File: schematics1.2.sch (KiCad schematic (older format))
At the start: 26 parts, among them J1 Keypad, SW1 SW_SPST, SW2 SW_SPST, SW3 SW_SPST, SW4 SW_SPST, U1 EA_T123X-I2C

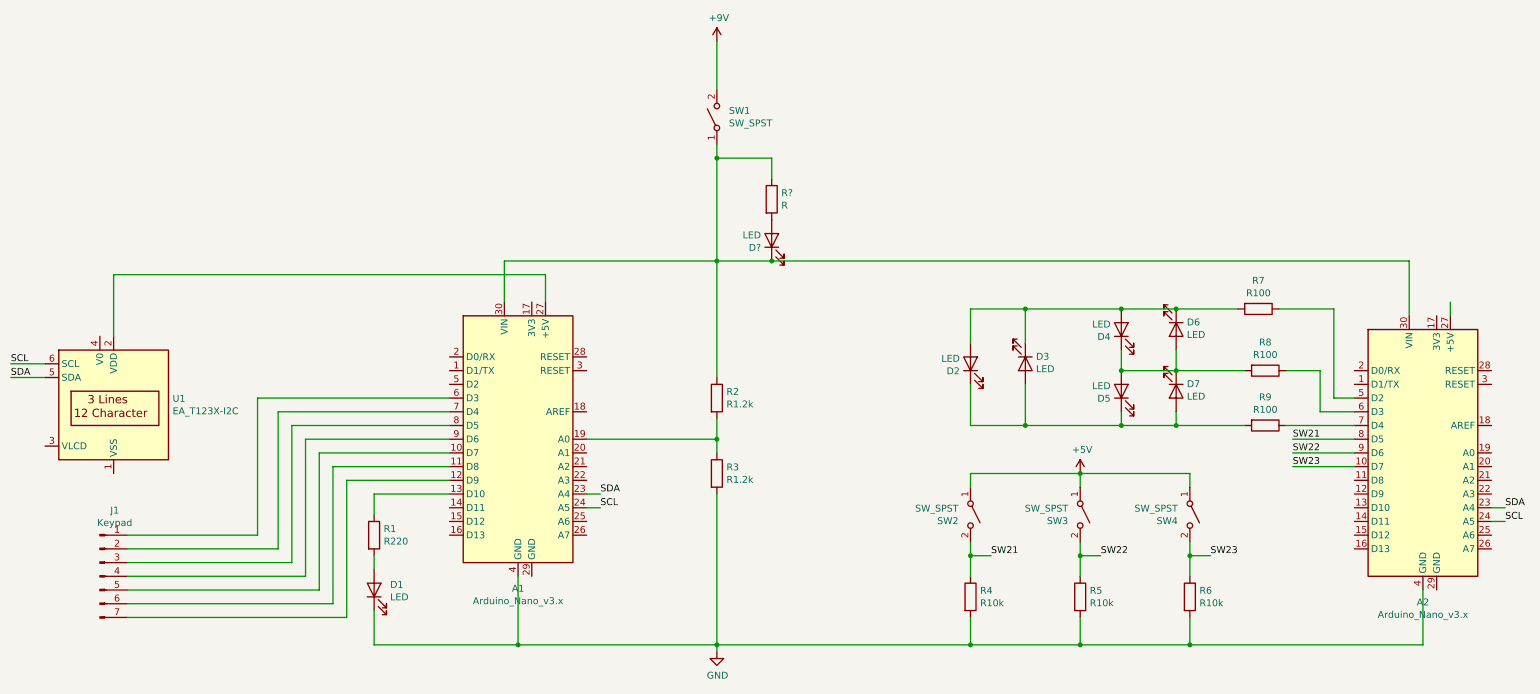
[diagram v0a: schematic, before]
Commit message: Removed second Nano, moved all components onto the one board. The second board is not required
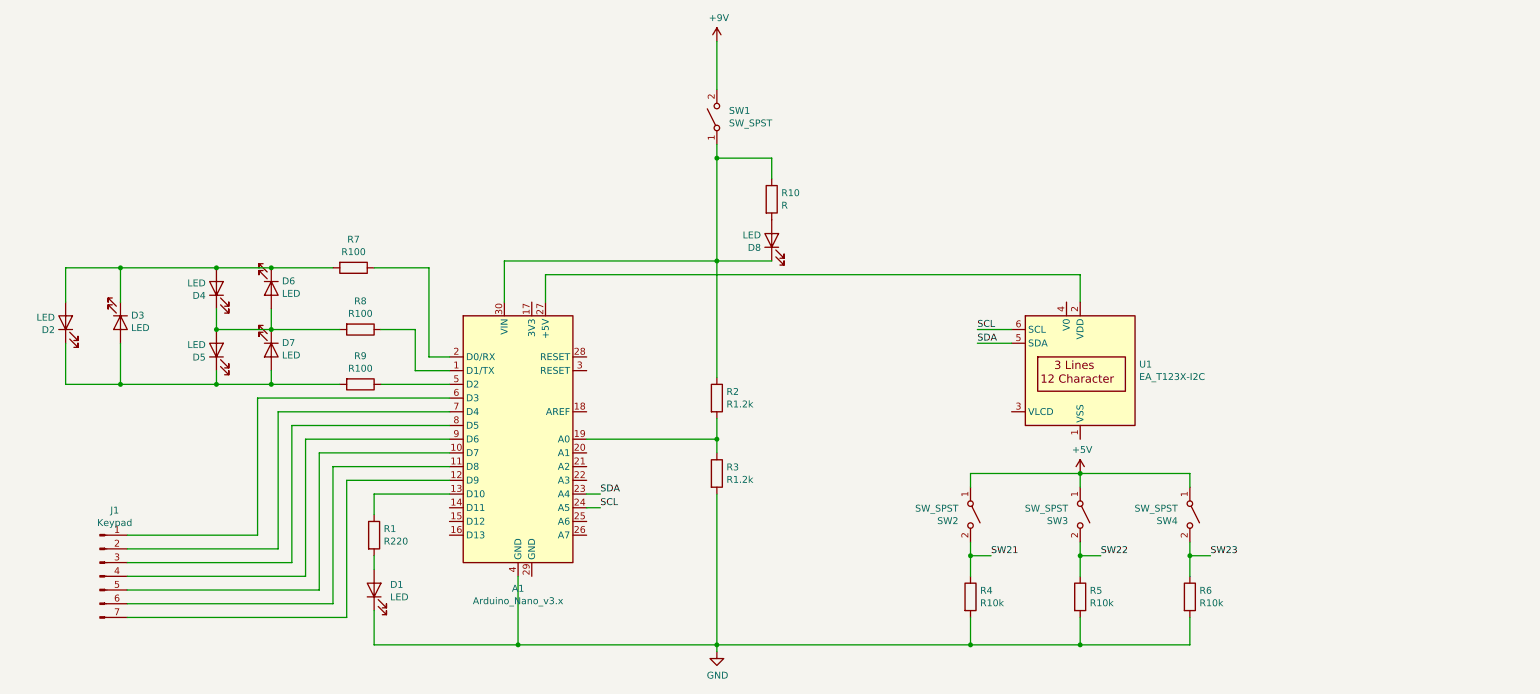
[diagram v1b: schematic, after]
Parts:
- removed A2: Arduino_Nano_v3.x, Module:Arduino_Nano, symbol MCU_Module:Arduino_Nano_v3.x
- gave numbers to parts that had none: 2
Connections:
- net at A1.1 (D1/TX): now also R8.1
- net at A1.2 (D0/RX): now also R7.1
- net at A1.5 (D2): now also R9.1
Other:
- moved on the sheet: D2, D3, D4, D5, D6, D7, R7, R8, R9, U1
